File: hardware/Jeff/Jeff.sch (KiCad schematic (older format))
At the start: 1 part

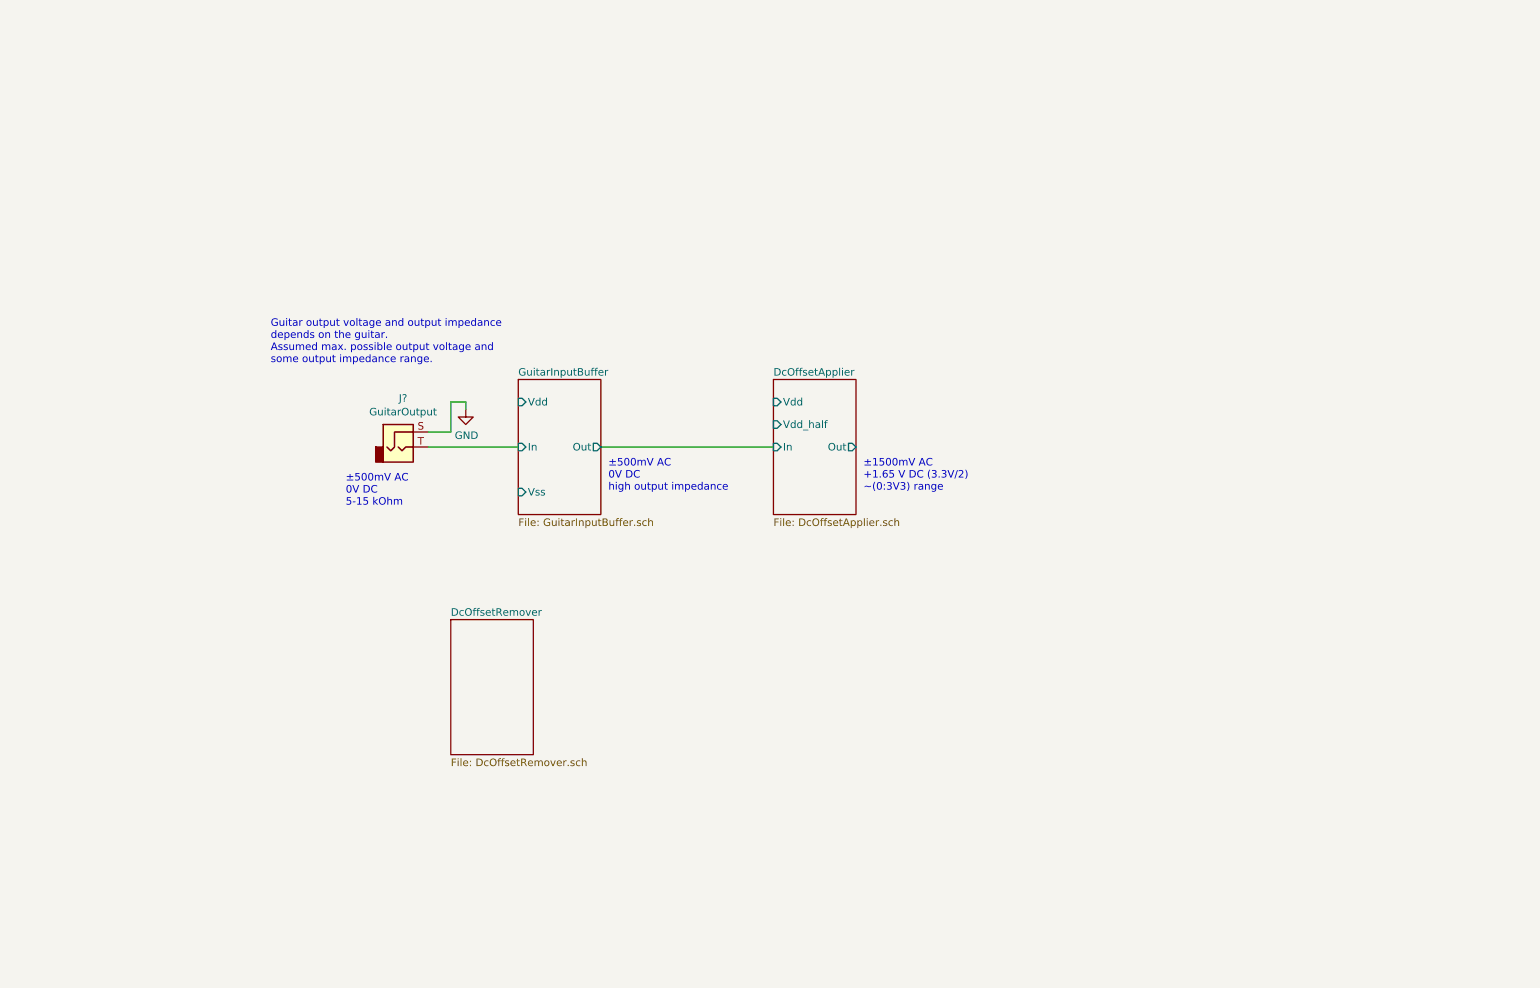
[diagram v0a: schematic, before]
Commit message: Add Analog Front End schematic, without miscs
The miscellanuous things I mean are the half-VCC splitter, VDD line,
negative voltage maker.
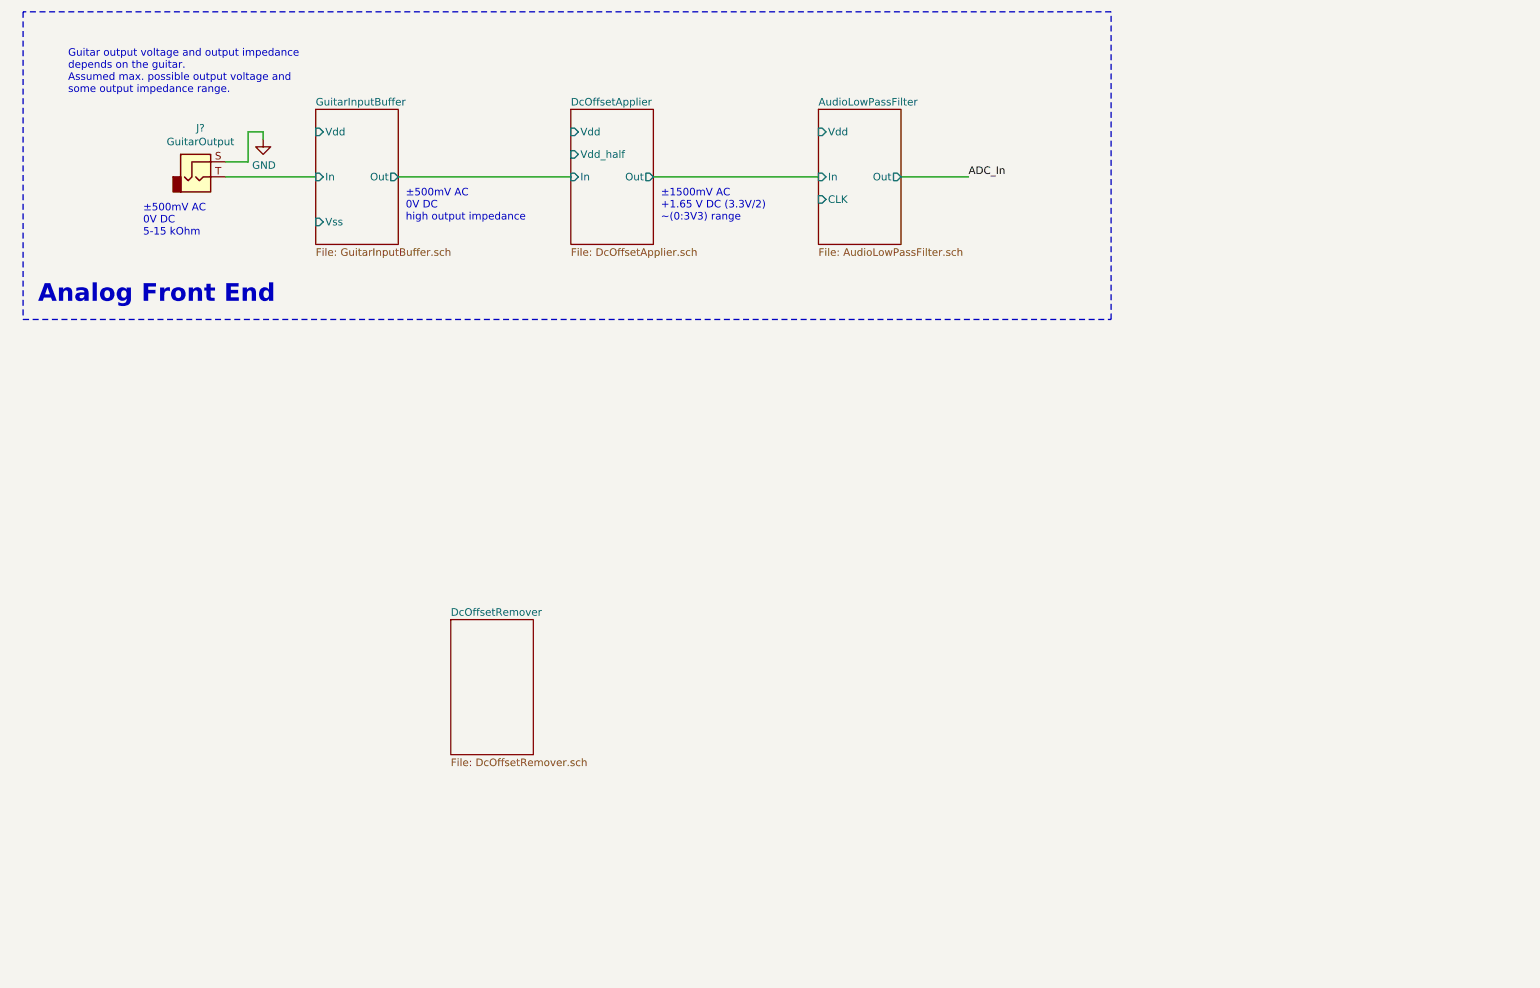
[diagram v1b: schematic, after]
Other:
- note added: "Analog Front End"
- moved on the sheet: J?
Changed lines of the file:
@@
 $Descr A4 11693 8268
 encoding utf-8
-Sheet 1 4
+Sheet 1 5
 Title ""
 Date ""
@@
 L Connector:AudioJack2 J?
 U 1 1 62166804
-P 3500 3700
-F 0 "J?" H 3532 4025 50  0000 C CNN
-F 1 "GuitarOutput" H 3532 3934 50  0000 C CNN
-F 2 "" H 3500 3700 50  0001 C CNN
-F 3 "~" H 3500 3700 50  0001 C CNN
-	1    3500 3700
+P 2150 1900
+F 0 "J?" H 2182 2225 50  0000 C CNN
+F 1 "GuitarOutput" H 2182 2134 50  0000 C CNN
+F 2 "" H 2150 1900 50  0001 C CNN
+F 3 "~" H 2150 1900 50  0001 C CNN
+	1    2150 1900
 	1    0    0    -1
 $EndComp
 $Sheet
-S 4300 3250 550  900
+S 2950 1450 550  900
 U 62166F90
 F0 "GuitarInputBuffer" 50
 F1 "GuitarInputBuffer.sch" 50
-F2 "In" I L 4300 3700 50
-F3 "Out" O R 4850 3700 50
-F4 "Vss" I L 4300 4000 50
-F5 "Vdd" I L 4300 3400 50
+F2 "In" I L 2950 1900 50
+F3 "Out" O R 3500 1900 50
+F4 "Vss" I L 2950 2200 50
+F5 "Vdd" I L 2950 1600 50
 $EndSheet
 $Comp
 L power:GND #PWR?
 U 1 1 6216A036
-P 3950 3450
-F 0 "#PWR?" H 3950 3200 50  0001 C CNN
-F 1 "GND" H 3955 3277 50  0000 C CNN
-F 2 "" H 3950 3450 50  0001 C CNN
-F 3 "" H 3950 3450 50  0001 C CNN
-	1    3950 3450
+P 2600 1650
+F 0 "#PWR?" H 2600 1400 50  0001 C CNN
+F 1 "GND" H 2605 1477 50  0000 C CNN
+F 2 "" H 2600 1650 50  0001 C CNN
+F 3 "" H 2600 1650 50  0001 C CNN
+	1    2600 1650
 	1    0    0    -1
 $EndComp
 Wire Wire Line
-	3700 3600 3850 3600
+	2350 1800 2500 1800
 Wire Wire Line
-	3850 3600 3850 3400
+	2500 1800 2500 1600
 Wire Wire Line
-	4300 3700 3700 3700
+	2950 1900 2350 1900
 Wire Wire Line
-	3950 3450 3950 3400
+	2600 1650 2600 1600
 Wire Wire Line
-	3950 3400 3850 3400
+	2600 1600 2500 1600
 $Sheet
 S 3850 4850 550  900
@@
 F1 "DcOffsetRemover.sch" 50
 $EndSheet
-Text Notes 3150 4100 0    50   ~ 0
+Text Notes 1800 2300 0    50   ~ 0
 ±500mV AC\n0V DC\n5-15 kOhm
 $Sheet
-S 6000 3250 550  900
+S 4650 1450 550  900
 U 6216D512
 F0 "DcOffsetApplier" 50
 F1 "DcOffsetApplier.sch" 50
-F2 "In" I L 6000 3700 50
-F3 "Vdd_half" I L 6000 3550 50
-F4 "Out" O R 6550 3700 50
-F5 "Vdd" I L 6000 3400 50
+F2 "In" I L 4650 1900 50
+F3 "Vdd_half" I L 4650 1750 50
+F4 "Out" O R 5200 1900 50
+F5 "Vdd" I L 4650 1600 50
 $EndSheet
 Wire Wire Line
-	4850 3700 6000 3700
-Text Notes 4900 4000 0    50   ~ 0
+	3500 1900 4650 1900
+Text Notes 3550 2200 0    50   ~ 0
 ±500mV AC\n0V DC\nhigh output impedance
-Text Notes 2650 3150 0    50   ~ 0
+Text Notes 1300 1350 0    50   ~ 0
 Guitar output voltage and output impedance\ndepends on the guitar.\nAssumed max. possible output voltage and\nsome output impedance range.
-Text Notes 6600 4000 0    50   ~ 0
+Text Notes 5250 2200 0    50   ~ 0
 ±1500mV AC\n+1.65 V DC (3.3V/2)\n~~(0:3V3) range
+$Sheet
+S 6300 1450 550  900
+U 621761CD
+F0 "AudioLowPassFilter" 50
+F1 "AudioLowPassFilter.sch" 50
+F2 "Vdd" I L 6300 1600 50
+F3 "In" I L 6300 1900 50
+F4 "CLK" I L 6300 2050 50
+F5 "Out" O R 6850 1900 50
+$EndSheet
+Wire Wire Line
+	6300 1900 5200 1900
+Wire Wire Line
+	6850 1900 7300 1900
+Text Label 7300 1900 0    50   ~ 0
+ADC_In
+Wire Notes Line
+	1000 800  1000 2850
+Wire Notes Line
+	1000 2850 8250 2850
+Wire Notes Line
+	8250 2850 8250 800
+Wire Notes Line
+	8250 800  1000 800
+Text Notes 1100 2750 0    118  ~ 24
+Analog Front End
 $EndSCHEMATC

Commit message: Add negative voltage generator schematic
This also connects the negative voltage to the analog front end.
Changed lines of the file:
@@
 $Descr A4 11693 8268
 encoding utf-8
-Sheet 1 5
+Sheet 1 6
 Title ""
 Date ""
@@
 	2600 1600 2500 1600
 $Sheet
-S 3850 4850 550  900
+S 6850 3450 550  900
 U 6216C0D1
 F0 "DcOffsetRemover" 50
@@
 Text Notes 1100 2750 0    118  ~ 24
 Analog Front End
+$Comp
+L power:+3.3V #PWR?
+U 1 1 6219044E
+P 2800 1550
+F 0 "#PWR?" H 2800 1400 50  0001 C CNN
+F 1 "+3.3V" H 2815 1723 50  0000 C CNN
+F 2 "" H 2800 1550 50  0001 C CNN
+F 3 "" H 2800 1550 50  0001 C CNN
+	1    2800 1550
+	1    0    0    -1
+$EndComp
+Wire Wire Line
+	2950 1600 2800 1600
+Wire Wire Line
+	2800 1600 2800 1550
+$Comp
+L power:+3.3V #PWR?
+U 1 1 62191985
+P 4500 1550
+F 0 "#PWR?" H 4500 1400 50  0001 C CNN
+F 1 "+3.3V" H 4515 1723 50  0000 C CNN
+F 2 "" H 4500 1550 50  0001 C CNN
+F 3 "" H 4500 1550 50  0001 C CNN
+	1    4500 1550
+	1    0    0    -1
+$EndComp
+Wire Wire Line
+	4650 1600 4500 1600
+Wire Wire Line
+	4500 1600 4500 1550
+$Comp
+L power:+3.3V #PWR?
+U 1 1 621932B2
+P 6150 1550
+F 0 "#PWR?" H 6150 1400 50  0001 C CNN
+F 1 "+3.3V" H 6165 1723 50  0000 C CNN
+F 2 "" H 6150 1550 50  0001 C CNN
+F 3 "" H 6150 1550 50  0001 C CNN
+	1    6150 1550
+	1    0    0    -1
+$EndComp
+Wire Wire Line
+	6300 1600 6150 1600
+Wire Wire Line
+	6150 1600 6150 1550
+$Sheet
+S 1300 6650 750  200
+U 6219438A
+F0 "NegativeVoltageGenerator" 50
+F1 "NegativeVoltageGenerator.sch" 50
+F2 "Vdd" I L 1300 6750 50
+F3 "-Vdd" O R 2050 6750 50
+$EndSheet
+$Comp
+L power:+3.3V #PWR?
+U 1 1 6219F15D
+P 1050 6650
+F 0 "#PWR?" H 1050 6500 50  0001 C CNN
+F 1 "+3.3V" H 1065 6823 50  0000 C CNN
+F 2 "" H 1050 6650 50  0001 C CNN
+F 3 "" H 1050 6650 50  0001 C CNN
+	1    1050 6650
+	1    0    0    -1
+$EndComp
+Wire Wire Line
+	1300 6750 1050 6750
+Wire Wire Line
+	1050 6750 1050 6650
+$Comp
+L power:-3V3 #PWR?
+U 1 1 6219FAA4
+P 2250 7000
+F 0 "#PWR?" H 2250 7100 50  0001 C CNN
+F 1 "-3V3" H 2265 7173 50  0000 C CNN
+F 2 "" H 2250 7000 50  0001 C CNN
+F 3 "" H 2250 7000 50  0001 C CNN
+	1    2250 7000
+	-1   0    0    1
+$EndComp
+Wire Wire Line
+	2050 6750 2250 6750
+Wire Wire Line
+	2250 6750 2250 7000
+$Comp
+L power:-3V3 #PWR?
+U 1 1 621A13F6
+P 2750 2300
+F 0 "#PWR?" H 2750 2400 50  0001 C CNN
+F 1 "-3V3" H 2765 2473 50  0000 C CNN
+F 2 "" H 2750 2300 50  0001 C CNN
+F 3 "" H 2750 2300 50  0001 C CNN
+	1    2750 2300
+	-1   0    0    1
+$EndComp
+Wire Wire Line
+	2950 2200 2750 2200
+Wire Wire Line
+	2750 2200 2750 2300
 $EndSCHEMATC

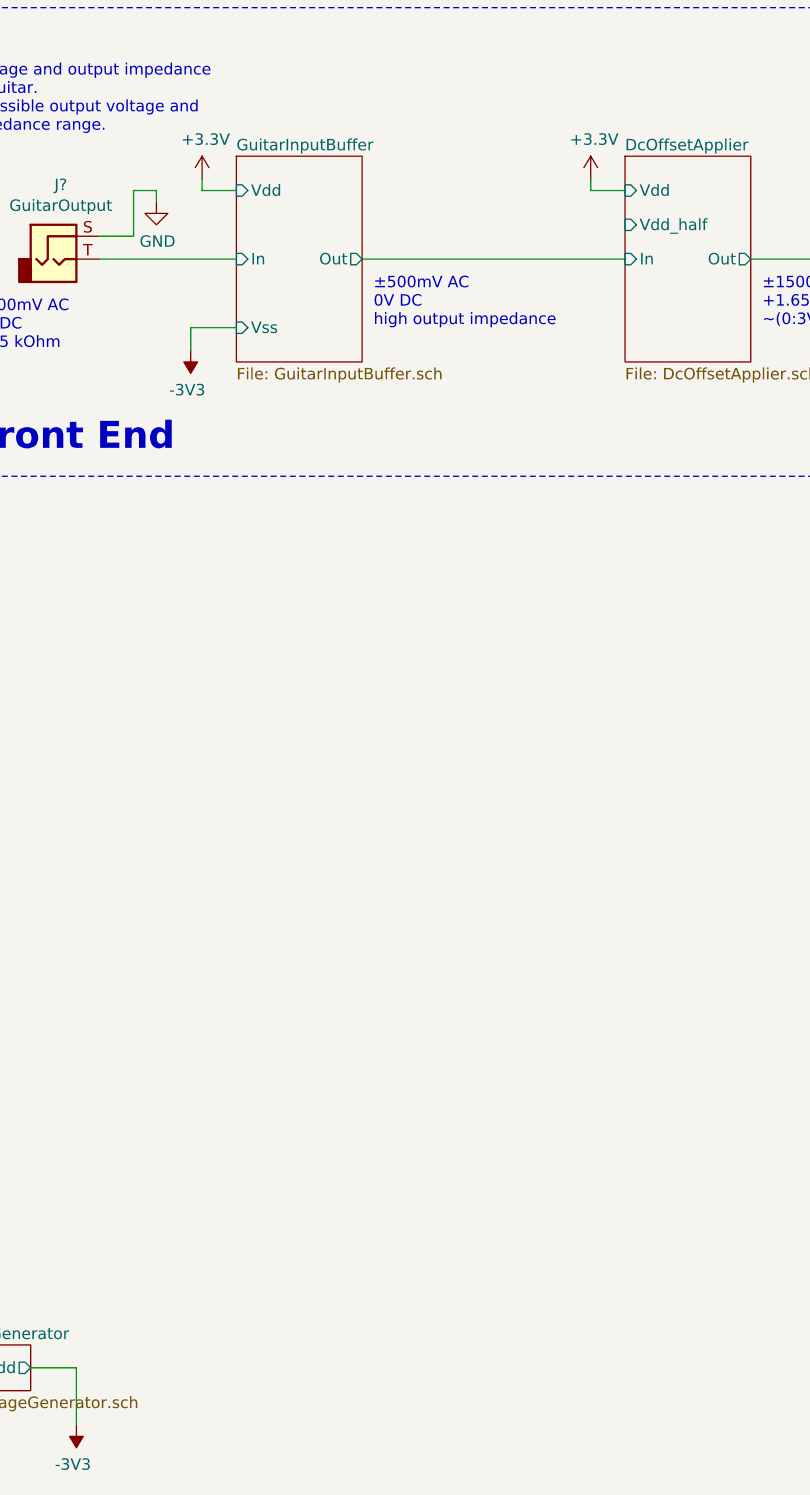
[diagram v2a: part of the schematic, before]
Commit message: Add VDD-half splitter
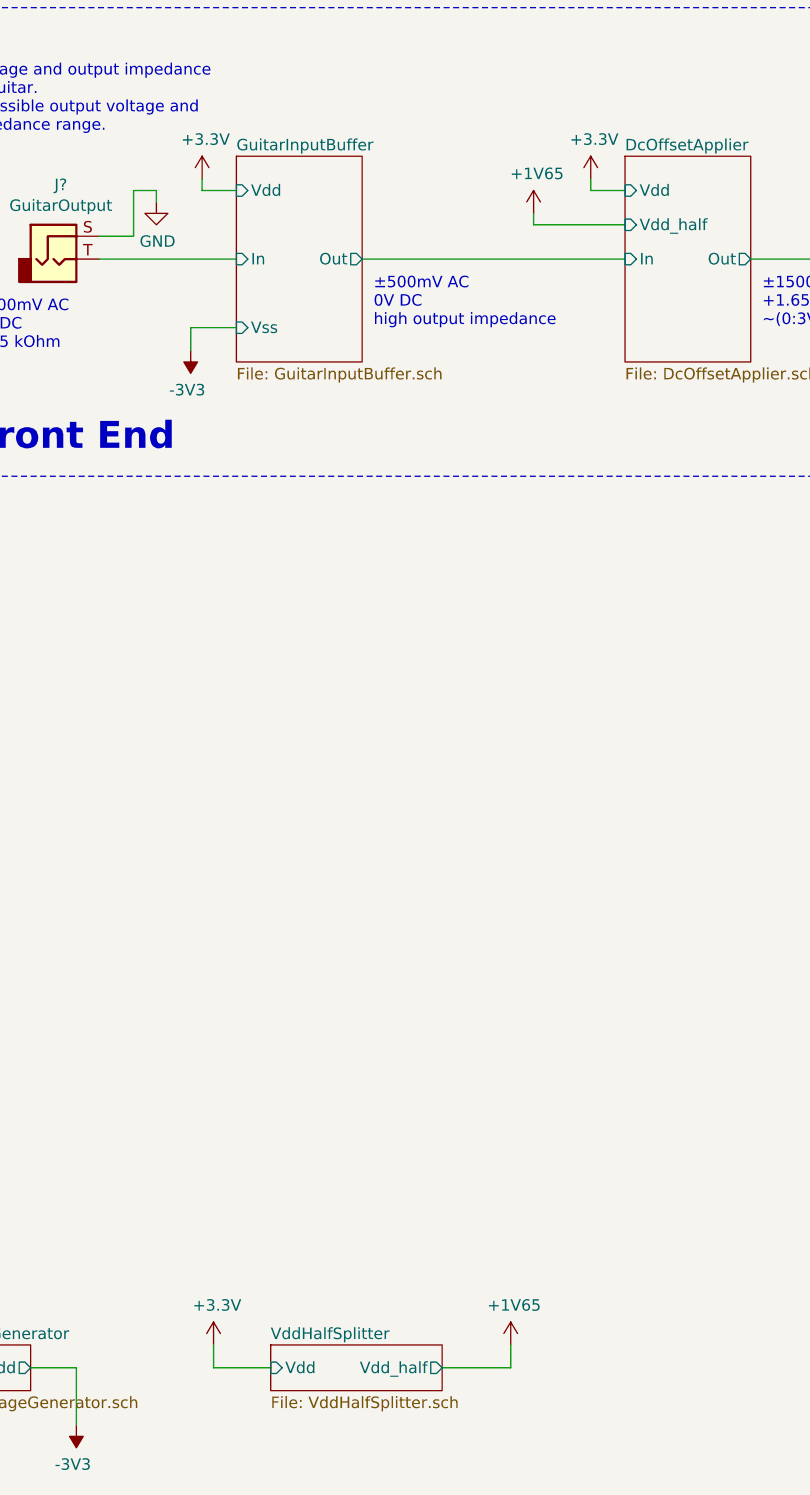
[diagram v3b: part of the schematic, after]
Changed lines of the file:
@@
 $Descr A4 11693 8268
 encoding utf-8
-Sheet 1 6
+Sheet 1 7
 Title ""
 Date ""
@@
 Wire Wire Line
 	2750 2200 2750 2300
+$Sheet
+S 3100 6650 750  200
+U 621A29F4
+F0 "VddHalfSplitter" 50
+F1 "VddHalfSplitter.sch" 50
+F2 "Vdd" I L 3100 6750 50
+F3 "Vdd_half" O R 3850 6750 50
+$EndSheet
+$Comp
+L power:+3.3V #PWR?
+U 1 1 621A9A4A
+P 2850 6650
+F 0 "#PWR?" H 2850 6500 50  0001 C CNN
+F 1 "+3.3V" H 2865 6823 50  0000 C CNN
+F 2 "" H 2850 6650 50  0001 C CNN
+F 3 "" H 2850 6650 50  0001 C CNN
+	1    2850 6650
+	1    0    0    -1
+$EndComp
+Wire Wire Line
+	3100 6750 2850 6750
+Wire Wire Line
+	2850 6750 2850 6650
+$Comp
+L PowerSources:+1V65 #PWR?
+U 1 1 621AA734
+P 4150 6650
+F 0 "#PWR?" H 4150 6500 50  0001 C CNN
+F 1 "+1V65" H 4165 6823 50  0000 C CNN
+F 2 "" H 4150 6650 50  0001 C CNN
+F 3 "" H 4150 6650 50  0001 C CNN
+	1    4150 6650
+	1    0    0    -1
+$EndComp
+Wire Wire Line
+	4150 6650 4150 6750
+Wire Wire Line
+	4150 6750 3850 6750
+$Comp
+L PowerSources:+1V65 #PWR?
+U 1 1 621AB60E
+P 4250 1700
+F 0 "#PWR?" H 4250 1550 50  0001 C CNN
+F 1 "+1V65" H 4265 1873 50  0000 C CNN
+F 2 "" H 4250 1700 50  0001 C CNN
+F 3 "" H 4250 1700 50  0001 C CNN
+	1    4250 1700
+	1    0    0    -1
+$EndComp
+Wire Wire Line
+	4250 1700 4250 1750
+Wire Wire Line
+	4650 1750 4250 1750
 $EndSCHEMATC
